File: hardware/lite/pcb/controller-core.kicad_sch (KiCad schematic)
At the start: 39 parts, among them J1101 SWD debug, SW1101 PTS645SL50SMTR92LFS, SW1102 PTS645SL50SMTR92LFS, U1101 RP2354B, Y1101 ABM8-272-T3

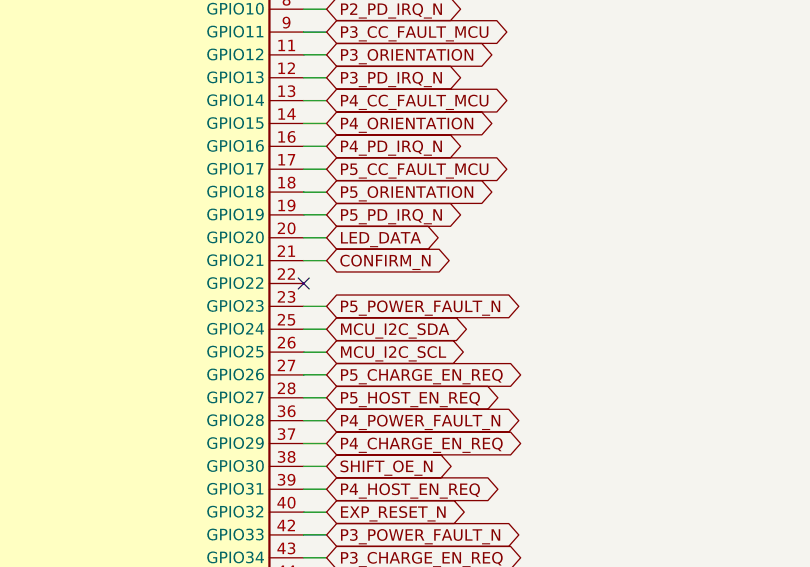
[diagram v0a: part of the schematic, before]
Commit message: feat(hardware): share brick power across ports and add CM5 link
A connected PD supply now runs the logic through its own buck and feeds
one TPS55288 buck-boost stage per port, so the contract is shared as
5-20 V at up to 5 A per port. The hub's VBUS detect becomes an OR gate,
a host-select mux lets a CM5 side board drive the hub over a 24-pin ZIF
link, and a CM5 variant joins Hub and HubPD.

The board is synced to the schematic and its old routing removed; the
new parts wait below the outline for placement.
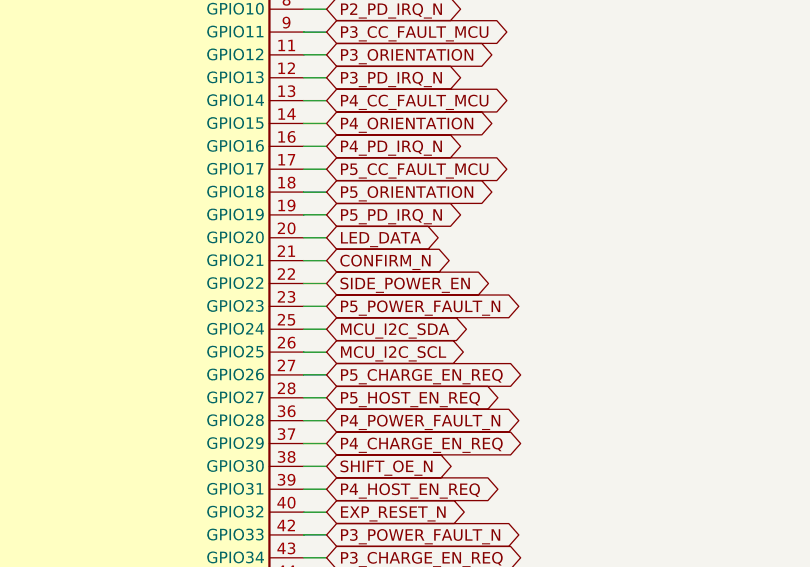
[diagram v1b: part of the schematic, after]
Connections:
- net SIDE_POWER_EN: now reaches U1101.22 (GPIO22)
- no-connect marks 7 -> 6

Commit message: feat(hardware): use smaller mux, I2C switch, 595 and button packages
The TMUX1511s move to UQFN-16 (RSV), the TCA9548A to VQFN-24 (RGE),
the 74HC595s to TSSOP-16 and the BOOTSEL and RESET buttons to the
Omron B3U, which frees about 300 mm2 of the middle band. The case
button keeps the PTS645.
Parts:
- SW1101, SW1102: value PTS645SL50SMTR92LFS -> B3U-1000P; footprint Button_Switch_SMD:SW_SPST_PTS645Sx43SMTR92 -> Button_Switch_SMD:SW_SPST_B3U-1000P; symbol Iasis:PTS645SL50SMTR92LFS -> Iasis:B3U-1000P; LCSC C221877 -> C231329; MPN PTS645SL50SMTR92LFS -> B3U-1000P; Manufacturer C&K -> Omron Electronics
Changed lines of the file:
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@@
 	)
 	(symbol
-		(lib_id "Iasis:PTS645SL50SMTR92LFS")
+		(lib_id "Iasis:B3U-1000P")
 		(at 88.9 231.14 270)
 		(unit 1)
@@
 			)
 		)
-		(property "Value" "PTS645SL50SMTR92LFS"
+		(property "Value" "B3U-1000P"
 			(at 86.36 232.41 90)
 			(show_name no)
@@
 			)
 		)
-		(property "Footprint" "Button_Switch_SMD:SW_SPST_PTS645Sx43SMTR92"
+		(property "Footprint" "Button_Switch_SMD:SW_SPST_B3U-1000P"
 			(at 88.9 214.63 0)
 			(hide yes)
@@
 			)
 		)
-		(property "Datasheet" "https://www.lcsc.com/datasheet/lcsc_datasheet_2304140030_C-K-PTS645SL50SMTR92LFS_C221877.pdf"
+		(property "Datasheet" "https://omronfs.omron.com/en_US/ecb/products/pdf/en-b3u.pdf"
 			(at 88.9 214.63 0)
 			(hide yes)
@@
 			)
 		)
-		(property "LCSC" "C221877"
+		(property "LCSC" "C231329"
 			(at 88.9 231.14 0)
 			(hide yes)
@@
 			)
 		)
-		(property "MPN" "PTS645SL50SMTR92LFS"
+		(property "MPN" "B3U-1000P"
 			(at 88.9 231.14 0)
 			(hide yes)
@@
 			)
 		)
-		(property "Manufacturer" "C&K"
+		(property "Manufacturer" "Omron Electronics"
 			(at 88.9 231.14 0)
 			(hide yes)
@@
 	)
 	(symbol
-		(lib_id "Iasis:PTS645SL50SMTR92LFS")
+		(lib_id "Iasis:B3U-1000P")
 		(at 114.3 231.14 270)
 		(unit 1)
@@
 			)
 		)
-		(property "Value" "PTS645SL50SMTR92LFS"
+		(property "Value" "B3U-1000P"
 			(at 119.38 232.41 90)
 			(show_name no)
@@
 			)
 		)
-		(property "Footprint" "Button_Switch_SMD:SW_SPST_PTS645Sx43SMTR92"
+		(property "Footprint" "Button_Switch_SMD:SW_SPST_B3U-1000P"
 			(at 114.3 214.63 0)
 			(hide yes)
@@
 			)
 		)
-		(property "Datasheet" "https://www.lcsc.com/datasheet/lcsc_datasheet_2304140030_C-K-PTS645SL50SMTR92LFS_C221877.pdf"
+		(property "Datasheet" "https://omronfs.omron.com/en_US/ecb/products/pdf/en-b3u.pdf"
 			(at 114.3 214.63 0)
 			(hide yes)
@@
 			)
 		)
-		(property "LCSC" "C221877"
+		(property "LCSC" "C231329"
 			(at 114.3 231.14 0)
 			(hide yes)
@@
 			)
 		)
-		(property "MPN" "PTS645SL50SMTR92LFS"
+		(property "MPN" "B3U-1000P"
 			(at 114.3 231.14 0)
 			(hide yes)
@@
 			)
 		)
-		(property "Manufacturer" "C&K"
+		(property "Manufacturer" "Omron Electronics"
 			(at 114.3 231.14 0)
 			(hide yes)
